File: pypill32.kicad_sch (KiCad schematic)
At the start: 44 parts, among them J1 HeaderR, J2 HeaderL, J3 USB_PINS, J4 SWD_HEADER, SW1 RST_BTN, SW2 BOOT_BTN, U1 SRV05-4, U2 PY32F030F18P6, U3 CH340N, U4 AMS1117-3.3, Y1 32.768 kHz

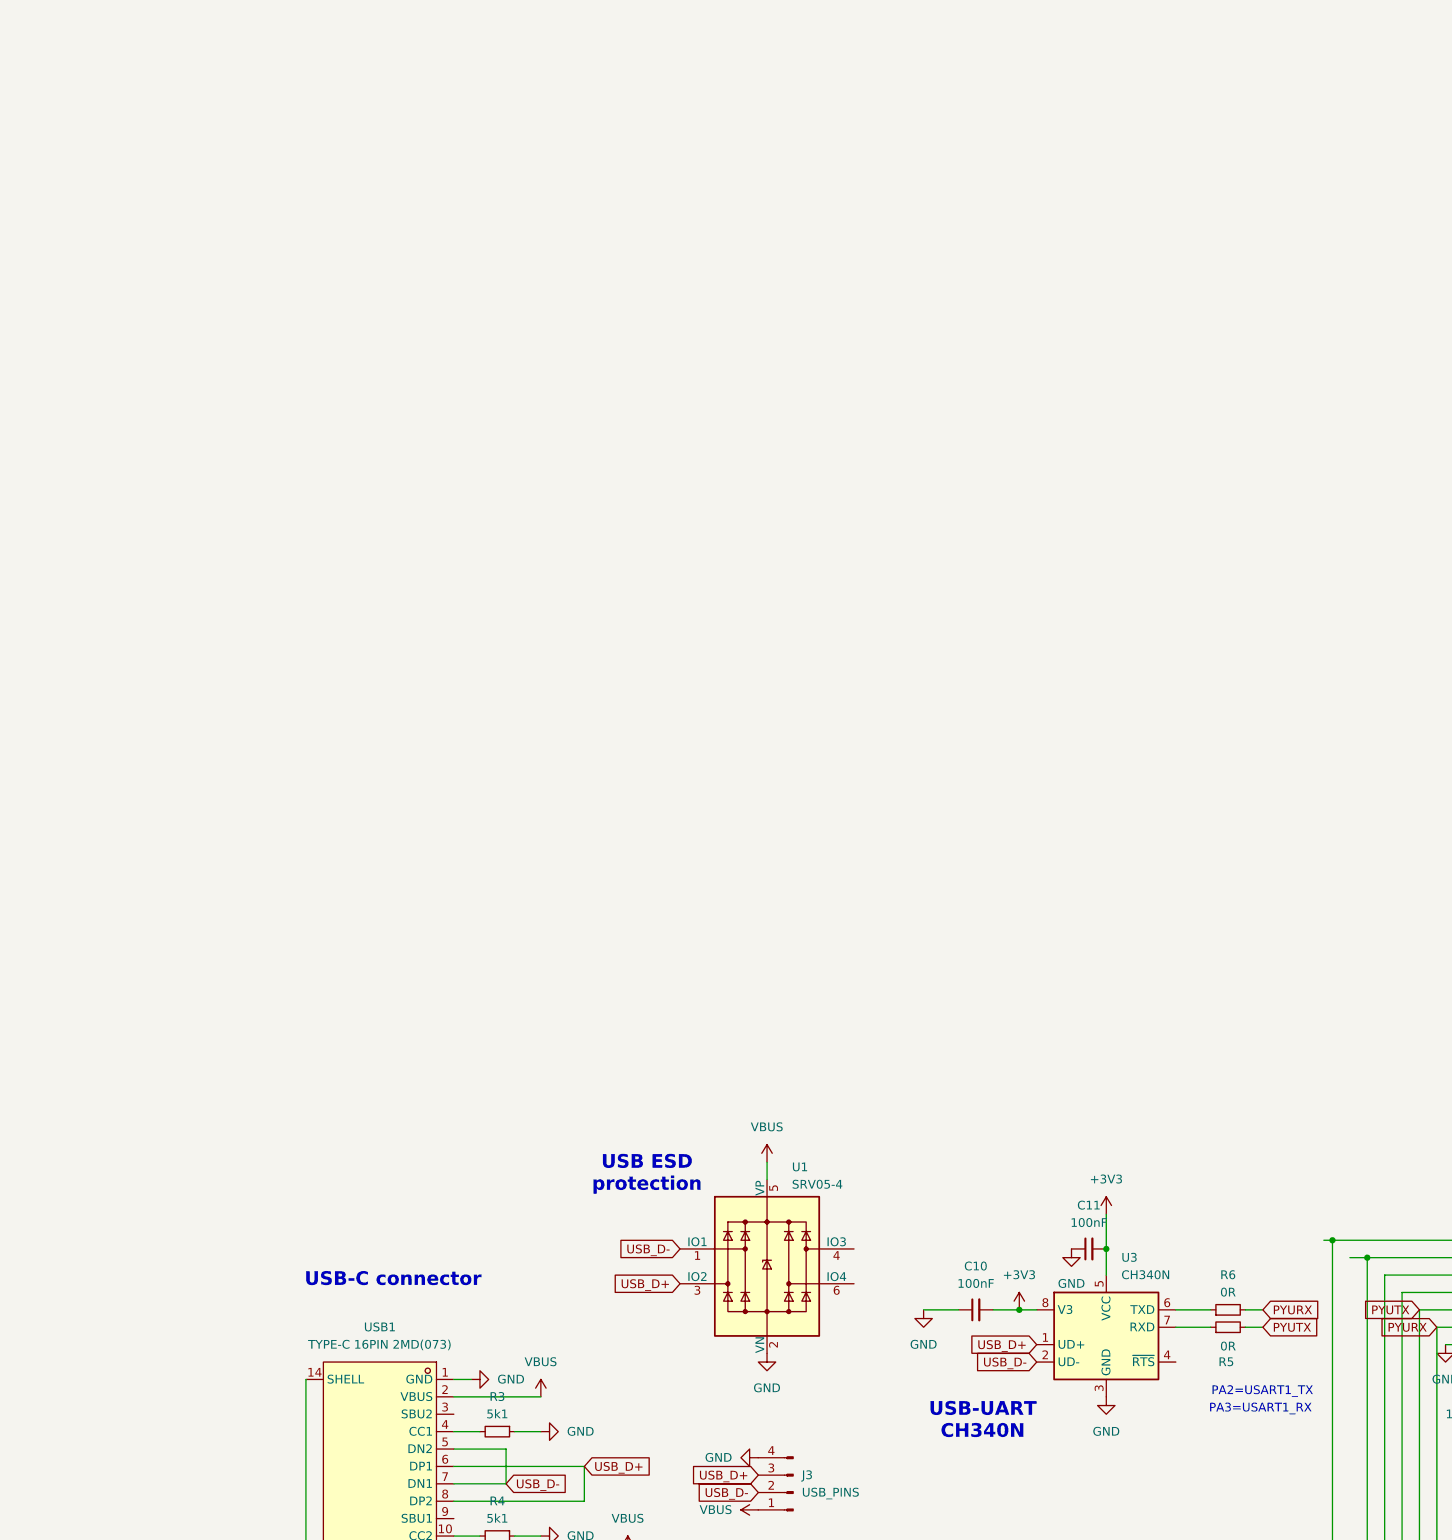
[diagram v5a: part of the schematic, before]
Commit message: added pad for RTS pin
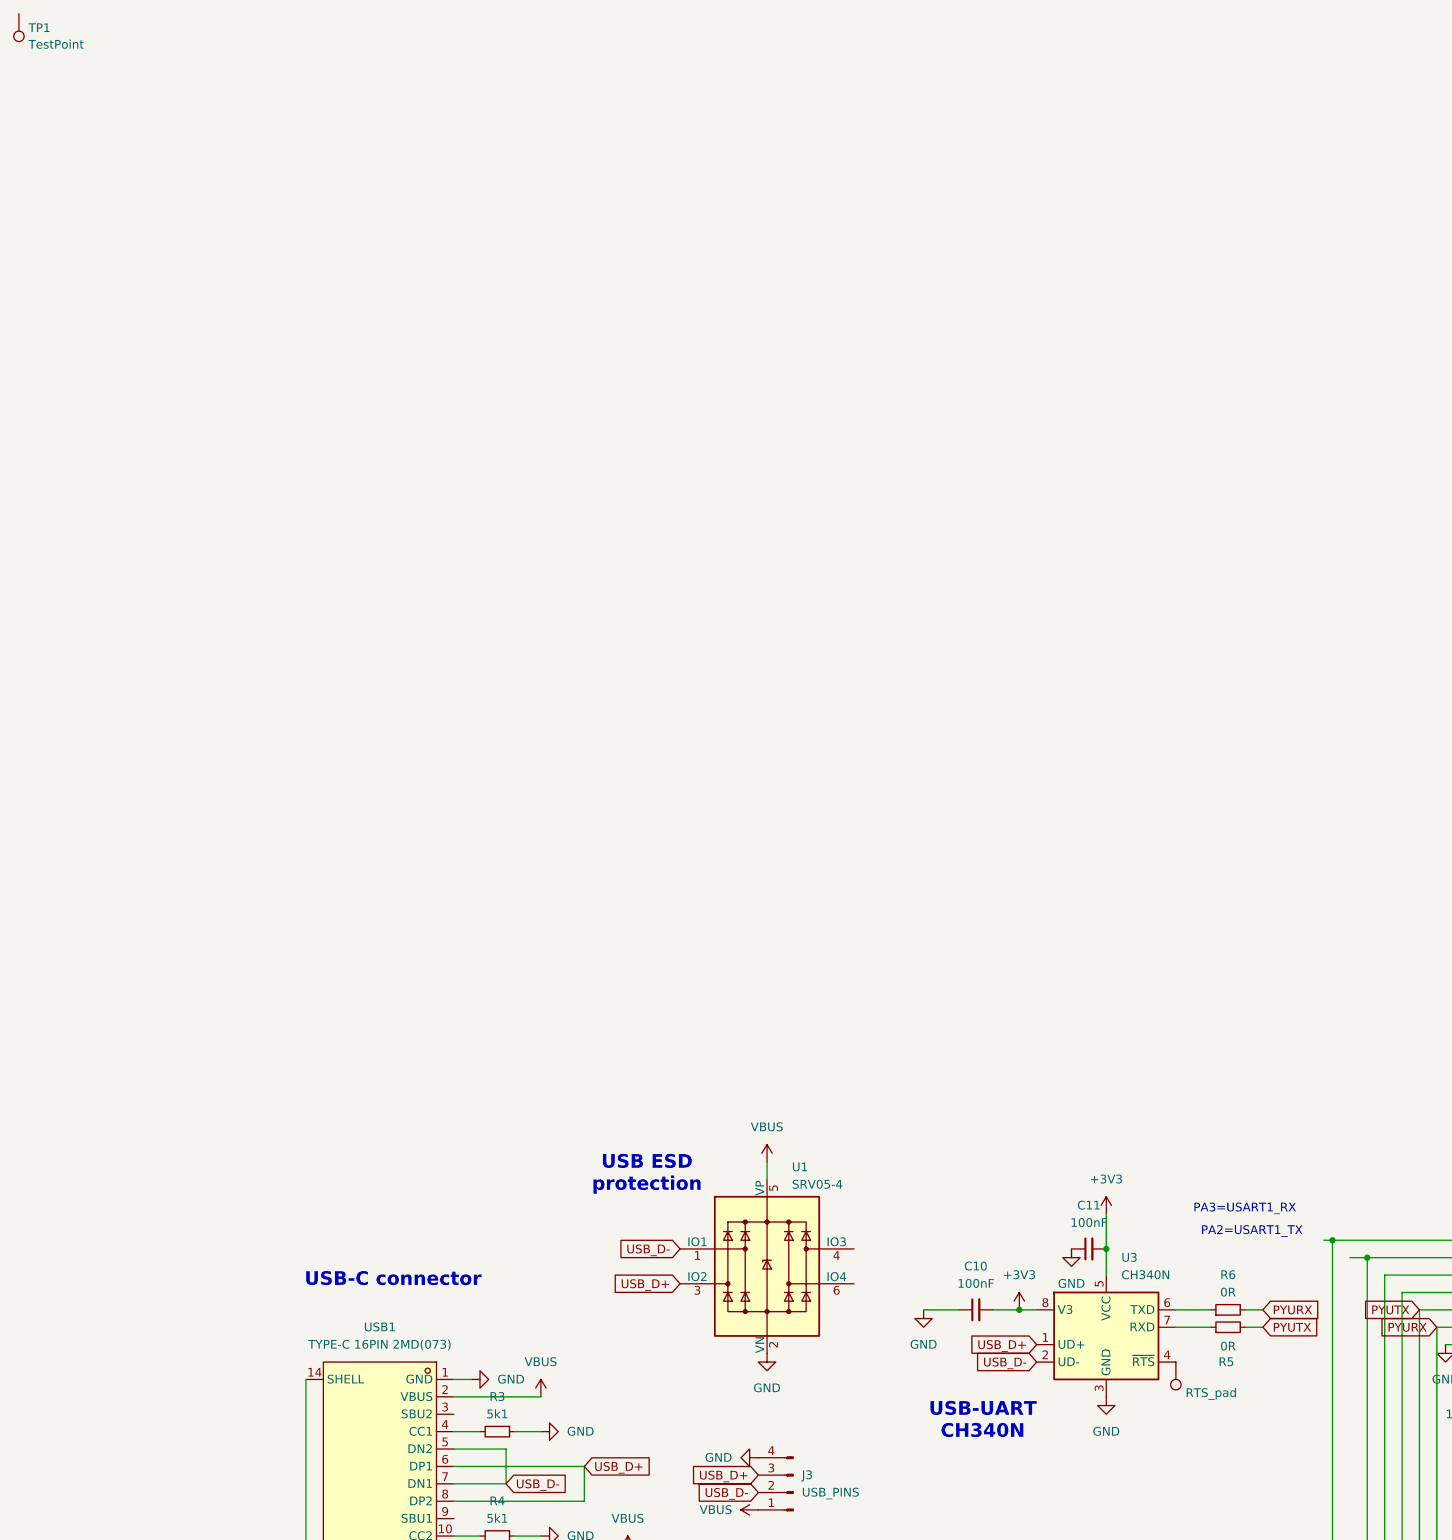
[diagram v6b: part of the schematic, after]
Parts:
- added TP1: TestPoint, symbol Connector:TestPoint
- added TP2: RTS_pad, TestPoint:TestPoint_Pad_D1.0mm, symbol Connector:TestPoint
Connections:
- net at U3.4 (~{RTS}): now also TP2.1
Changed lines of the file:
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@@
 	(text "PA3=USART1_RX"
 		(exclude_from_sim no)
-		(at 161.036 62.23 0)
+		(at 158.75 33.02 0)
 		(effects
 			(font
@@
 	(text "PA2=USART1_TX"
 		(exclude_from_sim no)
-		(at 176.276 59.69 0)
+		(at 174.752 36.322 0)
 		(effects
 			(font
@@
 	)
 	(symbol
+		(lib_id "Connector:TestPoint")
+		(at 156.21 54.61 180)
+		(unit 1)
+		(exclude_from_sim no)
+		(in_bom yes)
+		(on_board yes)
+		(dnp no)
+		(fields_autoplaced yes)
+		(property "Reference" "TP2"
+			(at 157.607 56.6998 0)
+			(effects
+				(font
+					(size 1.27 1.27)
+				)
+				(justify right)
+				(hide yes)
+			)
+		)
+		(property "Value" "RTS_pad"
+			(at 157.607 59.1241 0)
+			(effects
+				(font
+					(size 1.27 1.27)
+				)
+				(justify right)
+			)
+		)
+		(property "Footprint" "TestPoint:TestPoint_Pad_D1.0mm"
+			(at 151.13 54.61 0)
+			(effects
+				(font
+					(size 1.27 1.27)
+				)
+				(hide yes)
+			)
+		)
+		(property "Datasheet" "~"
+			(at 151.13 54.61 0)
+			(effects
+				(font
+					(size 1.27 1.27)
+				)
+				(hide yes)
+			)
+		)
+		(property "Description" "test point"
+			(at 156.21 54.61 0)
+			(effects
+				(font
+					(size 1.27 1.27)
+				)
+				(hide yes)
+			)
+		)
+		(pin "1"
+		)
+		(instances
+			(project ""
+				(path "/0471bd21-091d-469f-a793-0e3efa813f7b"
+					(reference "TP2")
+					(unit 1)
+				)
+			)
+		)
+	)
+	(symbol
 		(lib_id "Device:R_Small")
 		(at 163.83 46.99 90)
@@
 					(unit 1)
 				)
+			)
+		)
+	)
+	(symbol
+		(lib_id "Connector:TestPoint")
+		(at -12.7 -142.24 180)
+		(unit 1)
+		(exclude_from_sim no)
+		(in_bom yes)
+		(on_board yes)
+		(dnp no)
+		(fields_autoplaced yes)
+		(property "Reference" "TP1"
+			(at -11.303 -140.1502 0)
+			(effects
+				(font
+					(size 1.27 1.27)
+				)
+				(justify right)
+			)
+		)
+		(property "Value" "TestPoint"
+			(at -11.303 -137.7259 0)
+			(effects
+				(font
+					(size 1.27 1.27)
+				)
+				(justify right)
+			)
+		)
+		(property "Footprint" ""
+			(at -17.78 -142.24 0)
+			(effects
+				(font
+					(size 1.27 1.27)
+				)
+				(hide yes)
+			)
+		)
+		(property "Datasheet" "~"
+			(at -17.78 -142.24 0)
+			(effects
+				(font
+					(size 1.27 1.27)
+				)
+				(hide yes)
+			)
+		)
+		(property "Description" "test point"
+			(at -12.7 -142.24 0)
+			(effects
+				(font
+					(size 1.27 1.27)
+				)
+				(hide yes)
+			)
+		)
+		(pin "1"
+		)
+		(instances
+			(project ""
+				(path "/0471bd21-091d-469f-a793-0e3efa813f7b"
+					(reference "TP1")
+					(unit 1)
+				)

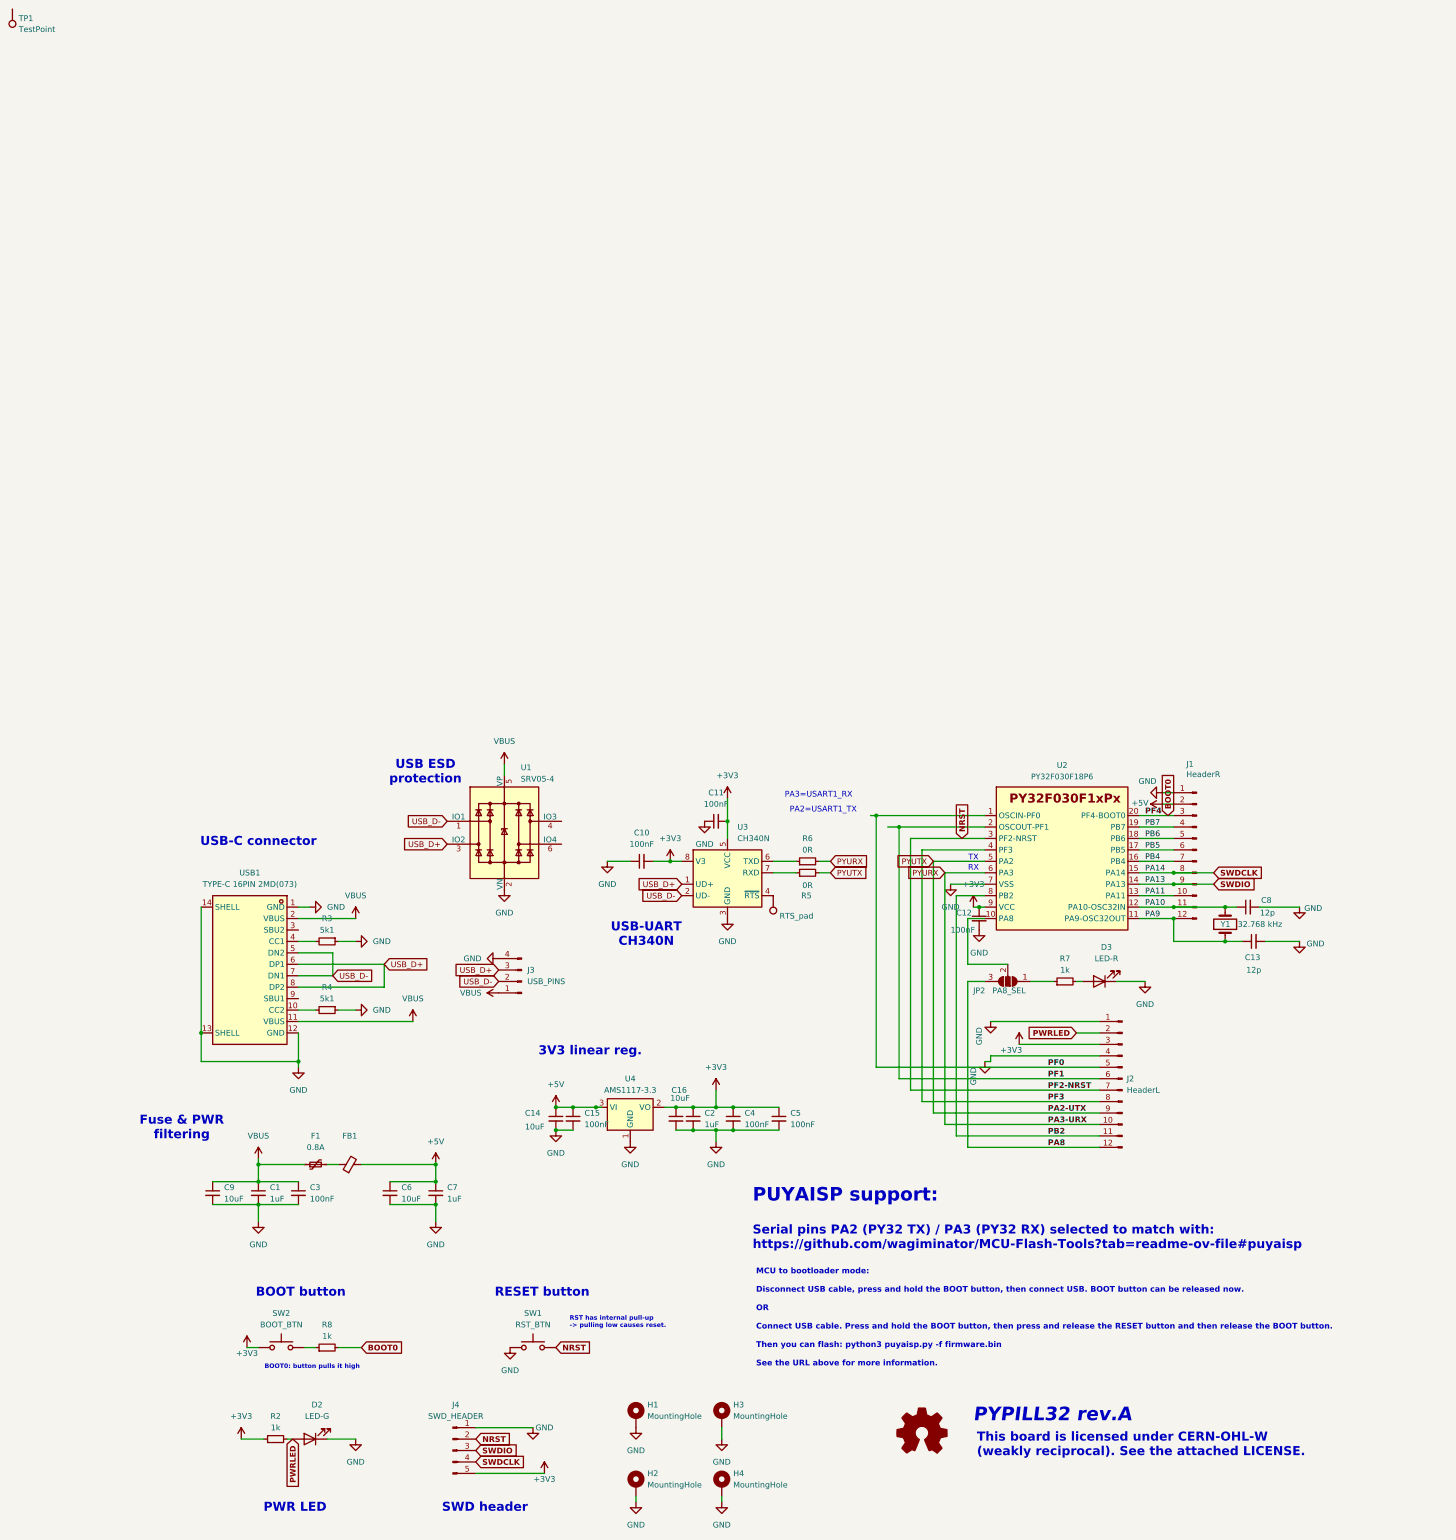
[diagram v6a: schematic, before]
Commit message: added HF crystal
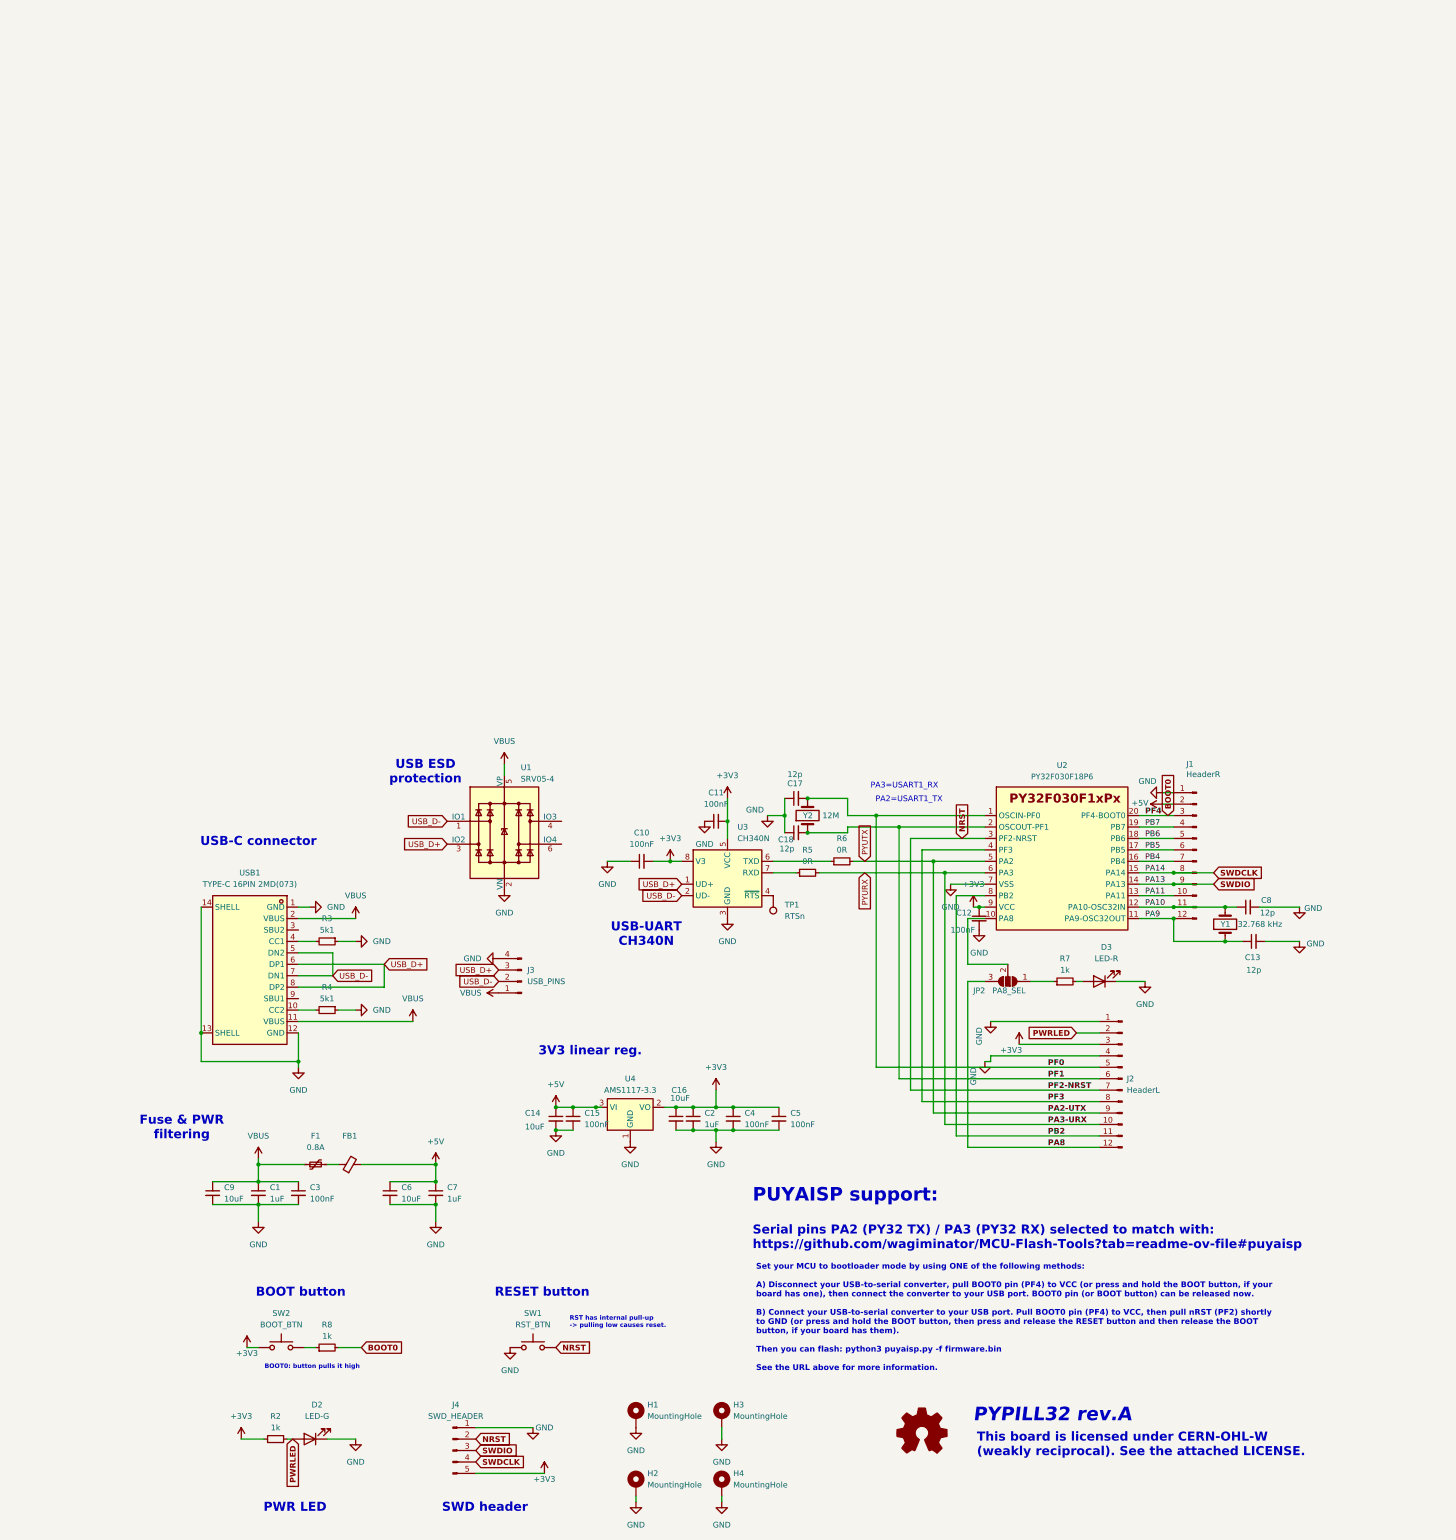
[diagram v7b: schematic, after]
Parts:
- removed TP2: RTS_pad, TestPoint:TestPoint_Pad_D1.0mm, symbol Connector:TestPoint
- added C17, C18: 12p, Capacitor_SMD:C_0805_2012Metric_Pad1.18x1.45mm_HandSolder, symbol Device:C_Small
- added Y2: 12M, Crystal:Crystal_HC49-4H_Vertical, symbol Device:Crystal
- TP1: value TestPoint -> RTSn; footprint (none) -> TestPoint:TestPoint_Pad_D1.0mm
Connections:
- net GND: now also C17.1, C18.1
- net PF0: now also C17.2, Y2.2
- net PF1: now also C18.2, Y2.1
- net PYURX: now also R5.2; no longer R6.2
- net PYUTX: now also R6.2; no longer R5.2
- net at U3.4 (~{RTS}): now also TP1.1
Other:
- note added: "Set your MCU to bootloader mode by using ONE of the following methods: A) Disconnect your USB-to-serial converter, pull BOOT0 pin (PF4) to VCC (or press and hold the BOOT button, if your board has one), then connect the converter to your USB port. BOOT0 pin (or BOOT button) can be released now. B) Connect your USB-to-serial converter to your USB port. Pull BOOT0 pin (PF4) to VCC, then pull nRST (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"
- note removed: "MCU to bootloader mode: Disconnect USB cable, press and hold the BOOT button, then connect USB. BOOT button can be released now. OR Connect USB cable. Press and hold the BOOT button, then press and release the RESET button and then release the BOOT button. Then you can flash: python3 puyaisp.py -f firmware.bin See the URL above for more information."
- note removed: "RX"
- note removed: "TX"
- moved on the sheet: R6
